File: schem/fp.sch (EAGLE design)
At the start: 12 parts, among them IC1 74HC244N, IC2 74HC244N, IC3 74HC244N, IC4 74HC244N, IC5 74HC377N, IC6 74HC244N, IC7 74HC244N, IC8 74HC244N

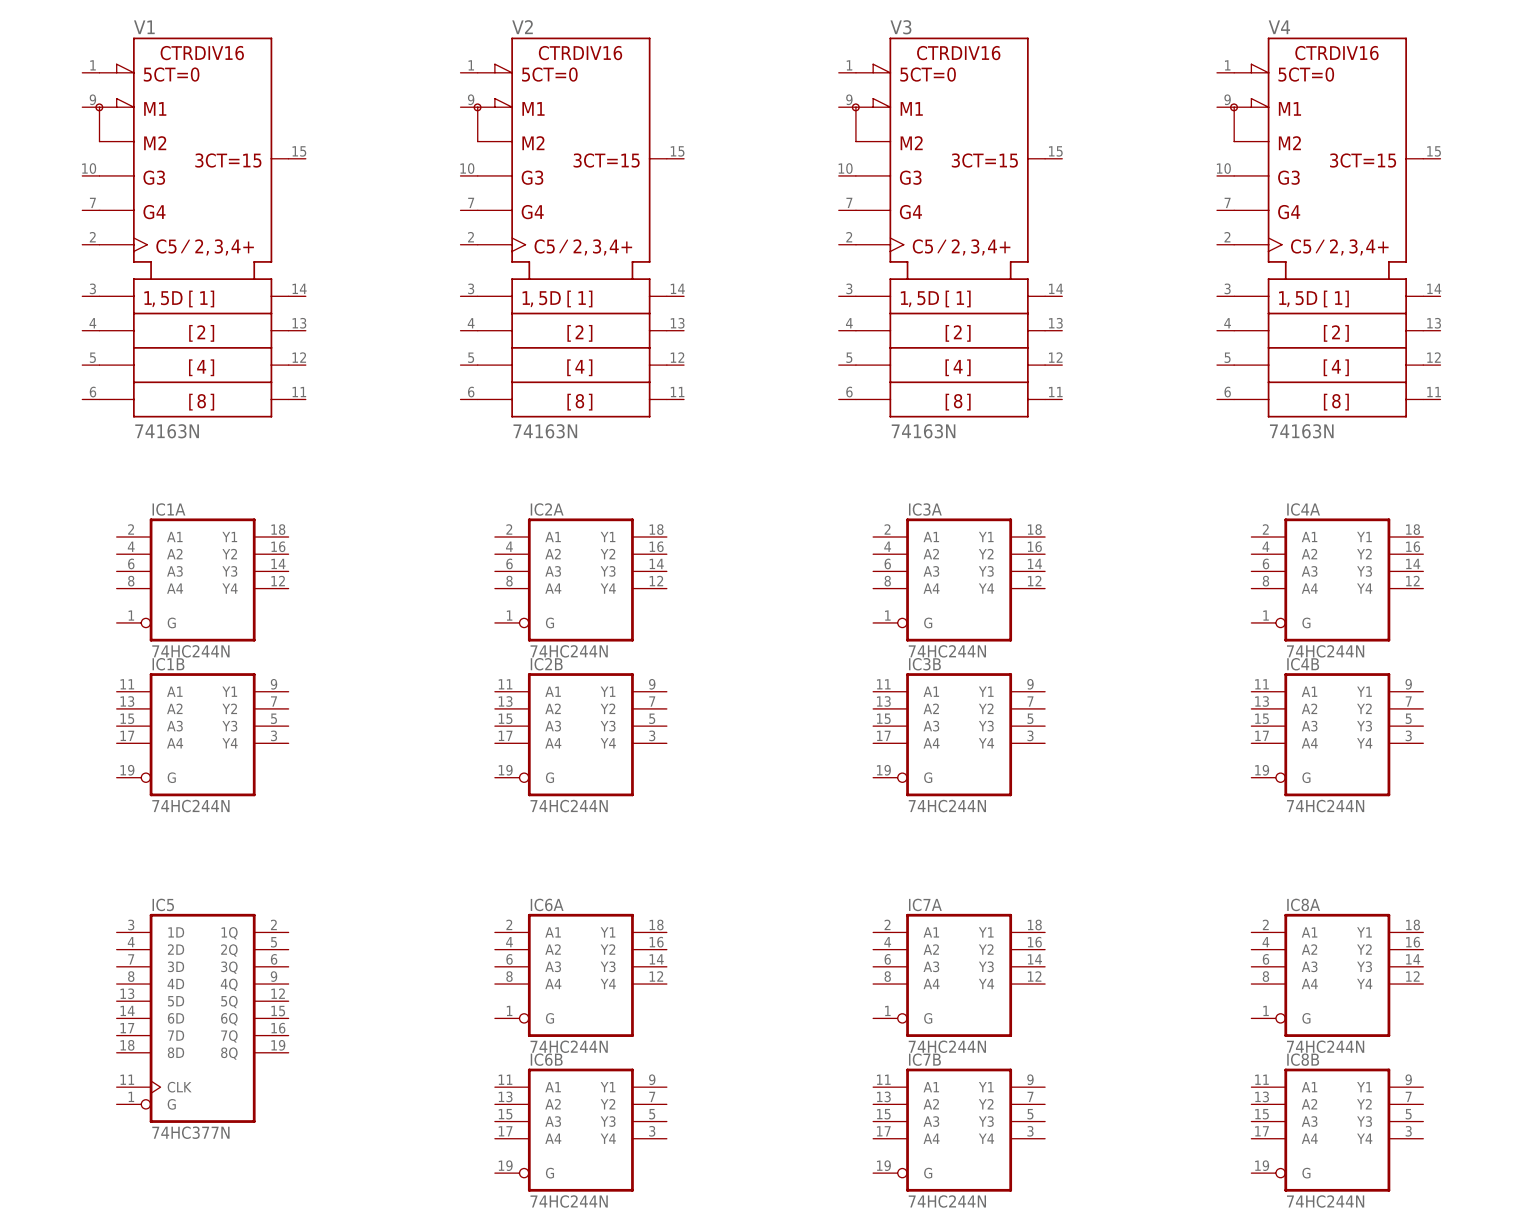
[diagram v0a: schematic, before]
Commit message: finished most schematics
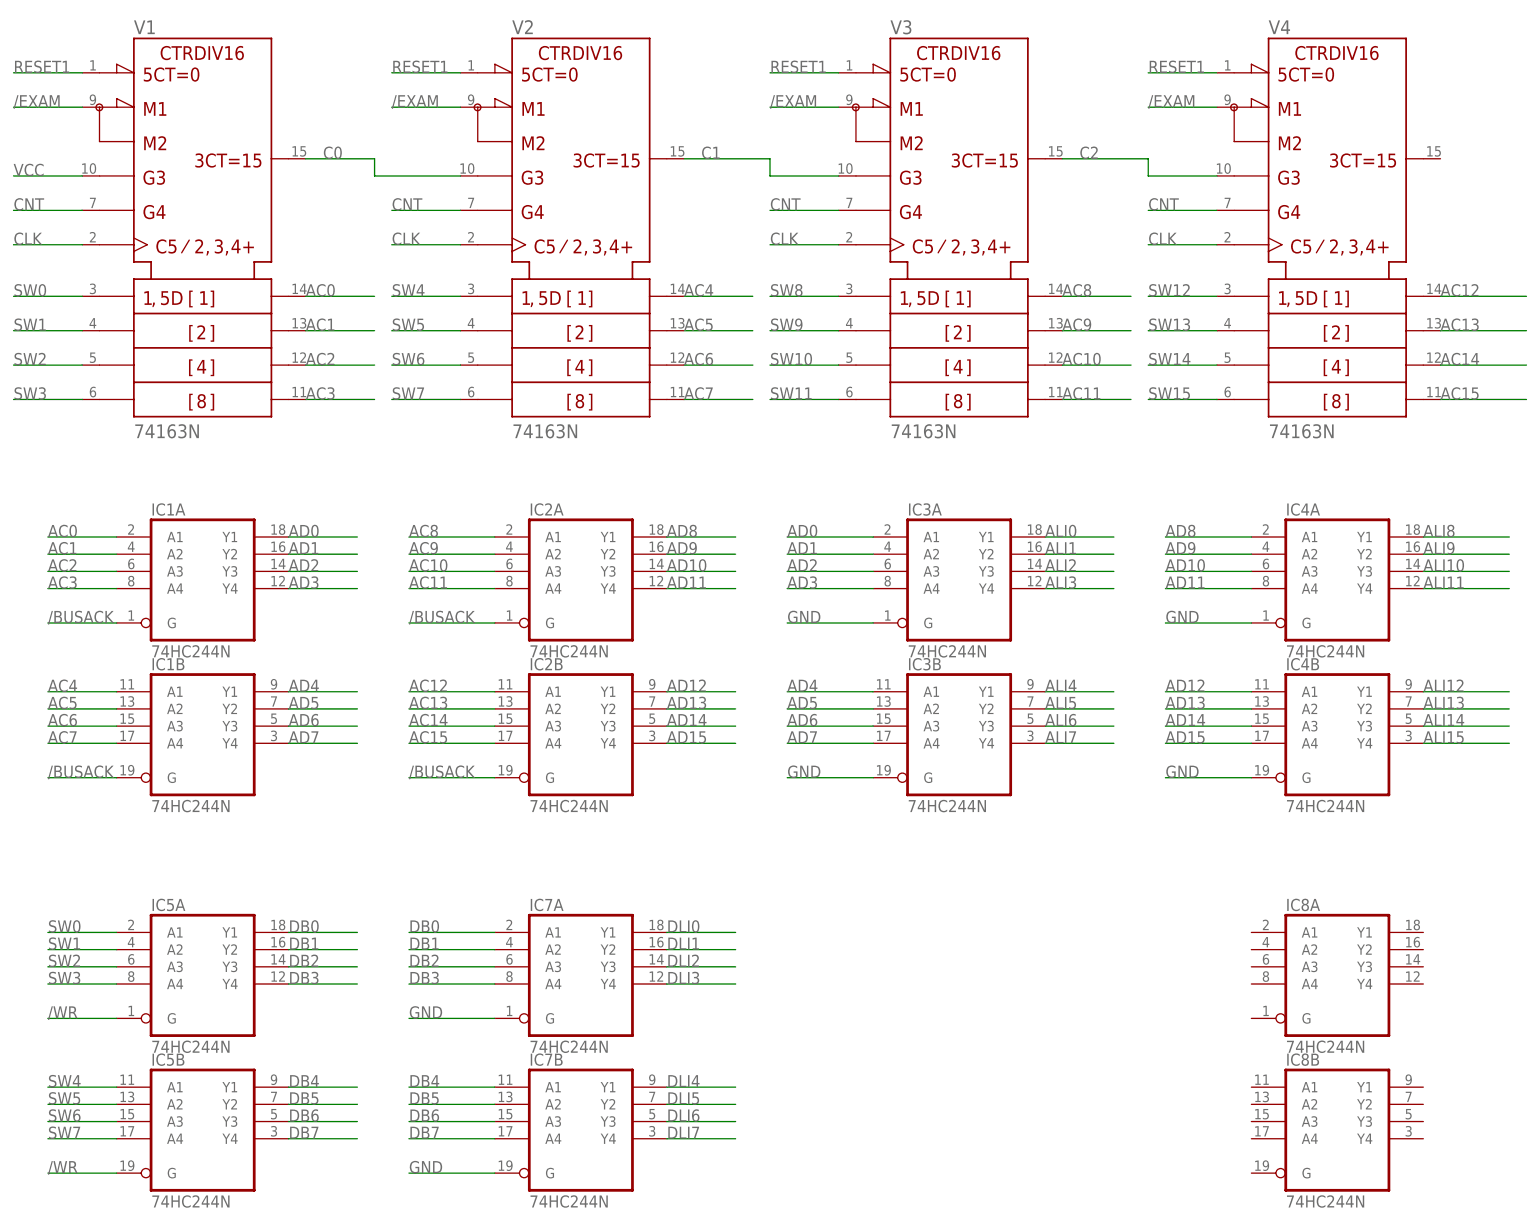
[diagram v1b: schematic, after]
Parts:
- removed IC6: 74HC244N, 74xx-eu:74HC244N
- IC5: value 74HC377N -> 74HC244N; device 74xx-eu:74HC377N -> 74xx-eu:74HC244N
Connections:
- new net /BUSACK: IC1A.G, IC1B.G, IC2A.G, IC2B.G
- new net /EXAM: V11.!LOAD, V21.!LOAD, V31.!LOAD, V41.!LOAD
- new net /WR: IC5A.G, IC5B.G
- new net AC0: IC1A.A1, V11.QA
- new net AC1: IC1A.A2, V11.QB
- new net AC10: IC2A.A3, V31.QC
- new net AC11: IC2A.A4, V31.QD
- new net AC12: IC2B.A1, V41.QA
- new net AC13: IC2B.A2, V41.QB
- new net AC14: IC2B.A3, V41.QC
- new net AC15: IC2B.A4, V41.QD
- new net AC2: IC1A.A3, V11.QC
- new net AC3: IC1A.A4, V11.QD
- new net AC4: IC1B.A1, V21.QA
- new net AC5: IC1B.A2, V21.QB
- new net AC6: IC1B.A3, V21.QC
- new net AC7: IC1B.A4, V21.QD
- new net AC8: IC2A.A1, V31.QA
- new net AC9: IC2A.A2, V31.QB
- new net AD0: IC1A.Y1, IC3A.A1
- new net AD1: IC1A.Y2, IC3A.A2
- new net AD10: IC2A.Y3, IC4A.A3
- new net AD11: IC2A.Y4, IC4A.A4
- new net AD12: IC2B.Y1, IC4B.A1
- new net AD13: IC2B.Y2, IC4B.A2
- new net AD14: IC2B.Y3, IC4B.A3
- new net AD15: IC2B.Y4, IC4B.A4
- new net AD2: IC1A.Y3, IC3A.A3
- new net AD3: IC1A.Y4, IC3A.A4
- new net AD4: IC1B.Y1, IC3B.A1
- new net AD5: IC1B.Y2, IC3B.A2
- new net AD6: IC1B.Y3, IC3B.A3
- new net AD7: IC1B.Y4, IC3B.A4
- new net AD8: IC2A.Y1, IC4A.A1
- new net AD9: IC2A.Y2, IC4A.A2
- new net ALI1: IC3A.Y2
- new net ALI10: IC4A.Y3
- new net ALI11: IC4A.Y4
- new net ALI12: IC4B.Y1
- new net ALI13: IC4B.Y2
- new net ALI14: IC4B.Y3
- new net ALI15: IC4B.Y4
- new net ALI2: IC3A.Y3
- new net ALI3: IC3A.Y4
- new net ALI4: IC3B.Y1
- new net ALI5: IC3B.Y2
- new net ALI6: IC3B.Y3
- new net ALI7: IC3B.Y4
- new net ALI8: IC4A.Y1
- new net ALI9: IC4A.Y2
- new net C0: V11.RCO, V21.ENT
- new net C1: V21.RCO, V31.ENT
- new net C2: V31.RCO, V41.ENT
- new net CLK: V11.CLK, V21.CLK, V31.CLK, V41.CLK
- new net CNT: V11.ENP, V21.ENP, V31.ENP, V41.ENP
- new net DB0: IC5A.Y1, IC7A.A1
- new net DB1: IC5A.Y2, IC7A.A2
- new net DB2: IC5A.Y3, IC7A.A3
- new net DB3: IC5A.Y4, IC7A.A4
- new net DB4: IC5B.Y1, IC7B.A1
- new net DB5: IC5B.Y2, IC7B.A2
- new net DB6: IC5B.Y3, IC7B.A3
- new net DB7: IC5B.Y4, IC7B.A4
- new net DLI0: IC7A.Y1
- new net DLI1: IC7A.Y2
- new net DLI2: IC7A.Y3
- new net DLI3: IC7A.Y4
- new net DLI4: IC7B.Y1
- new net DLI5: IC7B.Y2
- new net DLI6: IC7B.Y3
- new net DLI7: IC7B.Y4
- new net GND: IC3A.G, IC3B.G, IC4A.G, IC4B.G, IC7A.G, IC7B.G
- new net RESET1: V11.!CLR, V21.!CLR, V31.!CLR, V41.!CLR
- new net SW0: IC5A.A1, V11.A
- new net SW1: IC5A.A2, V11.B
- new net SW10: V31.C
- new net SW11: V31.D
- new net SW12: V41.A
- new net SW13: V41.B
- new net SW14: V41.C
- new net SW15: V41.D
- new net SW2: IC5A.A3, V11.C
- new net SW3: IC5A.A4, V11.D
- new net SW4: IC5B.A1, V21.A
- new net SW5: IC5B.A2, V21.B
- new net SW6: IC5B.A3, V21.C
- new net SW7: IC5B.A4, V21.D
- new net SW8: V31.A
- new net SW9: V31.B
- new net VCC: V11.ENT
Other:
- moved on the sheet: IC7A, IC7B

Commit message: more work on several fronts
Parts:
- removed IC4, IC5, IC7, IC8: 74HC244N, 74xx-eu:74HC244N
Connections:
- removed net ALI1: IC3A.Y2
- removed net ALI10: IC4A.Y3
- removed net ALI11: IC4A.Y4
- removed net ALI12: IC4B.Y1
- removed net ALI13: IC4B.Y2
- removed net ALI14: IC4B.Y3
- removed net ALI15: IC4B.Y4
- removed net ALI2: IC3A.Y3
- removed net ALI3: IC3A.Y4
- removed net ALI4: IC3B.Y1
- removed net ALI5: IC3B.Y2
- removed net ALI6: IC3B.Y3
- removed net ALI7: IC3B.Y4
- removed net ALI8: IC4A.Y1
- removed net ALI9: IC4A.Y2
- removed net DLI0: IC7A.Y1
- removed net DLI1: IC7A.Y2
- removed net DLI2: IC7A.Y3
- removed net DLI3: IC7A.Y4
- removed net DLI4: IC7B.Y1
- removed net DLI5: IC7B.Y2
- removed net DLI6: IC7B.Y3
- removed net DLI7: IC7B.Y4
- removed net GND: IC3A.G, IC3B.G, IC4A.G, IC4B.G, IC7A.G, IC7B.G
- net /WR: now also IC3A.G, IC3B.G; no longer IC5A.G, IC5B.G
- net AD0: no longer IC3A.A1
- net AD1: no longer IC3A.A2
- net AD10: no longer IC4A.A3
- net AD11: no longer IC4A.A4
- net AD12: no longer IC4B.A1
- net AD13: no longer IC4B.A2
- net AD14: no longer IC4B.A3
- net AD15: no longer IC4B.A4
- net AD2: no longer IC3A.A3
- net AD3: no longer IC3A.A4
- net AD4: no longer IC3B.A1
- net AD5: no longer IC3B.A2
- net AD6: no longer IC3B.A3
- net AD7: no longer IC3B.A4
- net AD8: no longer IC4A.A1
- net AD9: no longer IC4A.A2
- net DB0: now also IC3A.Y1; no longer IC5A.Y1, IC7A.A1
- net DB1: now also IC3A.Y2; no longer IC5A.Y2, IC7A.A2
- net DB2: now also IC3A.Y3; no longer IC5A.Y3, IC7A.A3
- net DB3: now also IC3A.Y4; no longer IC5A.Y4, IC7A.A4
- net DB4: now also IC3B.Y1; no longer IC5B.Y1, IC7B.A1
- net DB5: now also IC3B.Y2; no longer IC5B.Y2, IC7B.A2
- net DB6: now also IC3B.Y3; no longer IC5B.Y3, IC7B.A3
- net DB7: now also IC3B.Y4; no longer IC5B.Y4, IC7B.A4
- net SW0: now also IC3A.A1; no longer IC5A.A1
- net SW1: now also IC3A.A2; no longer IC5A.A2
- net SW2: now also IC3A.A3; no longer IC5A.A3
- net SW3: now also IC3A.A4; no longer IC5A.A4
- net SW4: now also IC3B.A1; no longer IC5B.A1
- net SW5: now also IC3B.A2; no longer IC5B.A2
- net SW6: now also IC3B.A3; no longer IC5B.A3
- net SW7: now also IC3B.A4; no longer IC5B.A4
